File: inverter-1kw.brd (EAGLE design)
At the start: 160 x 100 mm, 242 parts, among them IC1 LM358D, IC5 ISO3082, IC6 25LC080SN, IC9 LM358D, Q2 1200980569**TRANS SMD NPN MMB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, Q3 1200980569**TRANS SMD NPN MMB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, Q4 1200980569**TRANS SMD NPN MMB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, Q6 1200980569**TRANS SMD NPN MMB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, U1 ACS712, U2 STM32F334C6, U3 1039-2088**AM1L-0505SH30-NZ A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, U4 ACS712, U5 SI8230, U6 SI8230, U7 ACS712, X1 MCV3, X2 RADE2, X3 RADE2, X7 RADE2, X8 RADE2

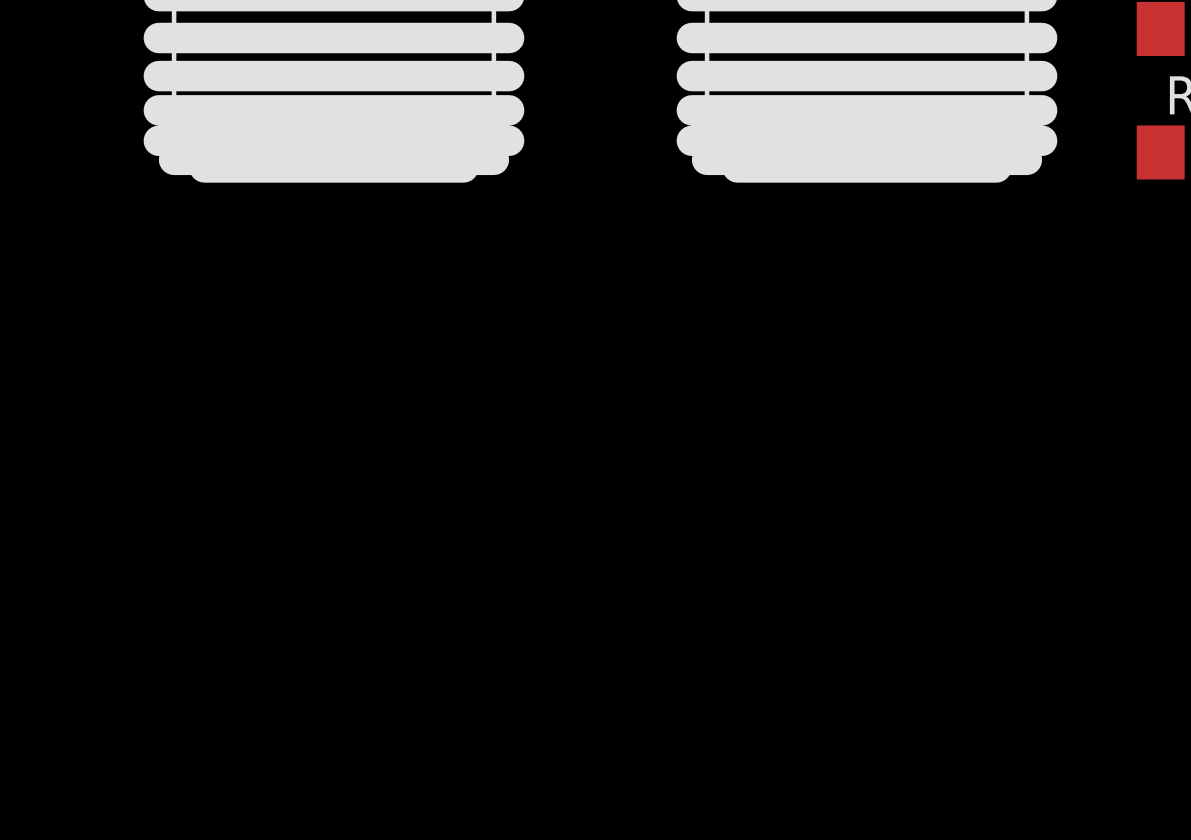
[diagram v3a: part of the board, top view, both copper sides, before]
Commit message: Cikis terminaline kondasator eklendi. Guc soketleri icin(4-pinli) kullanilacak urun linki value alanlarina yazildi.
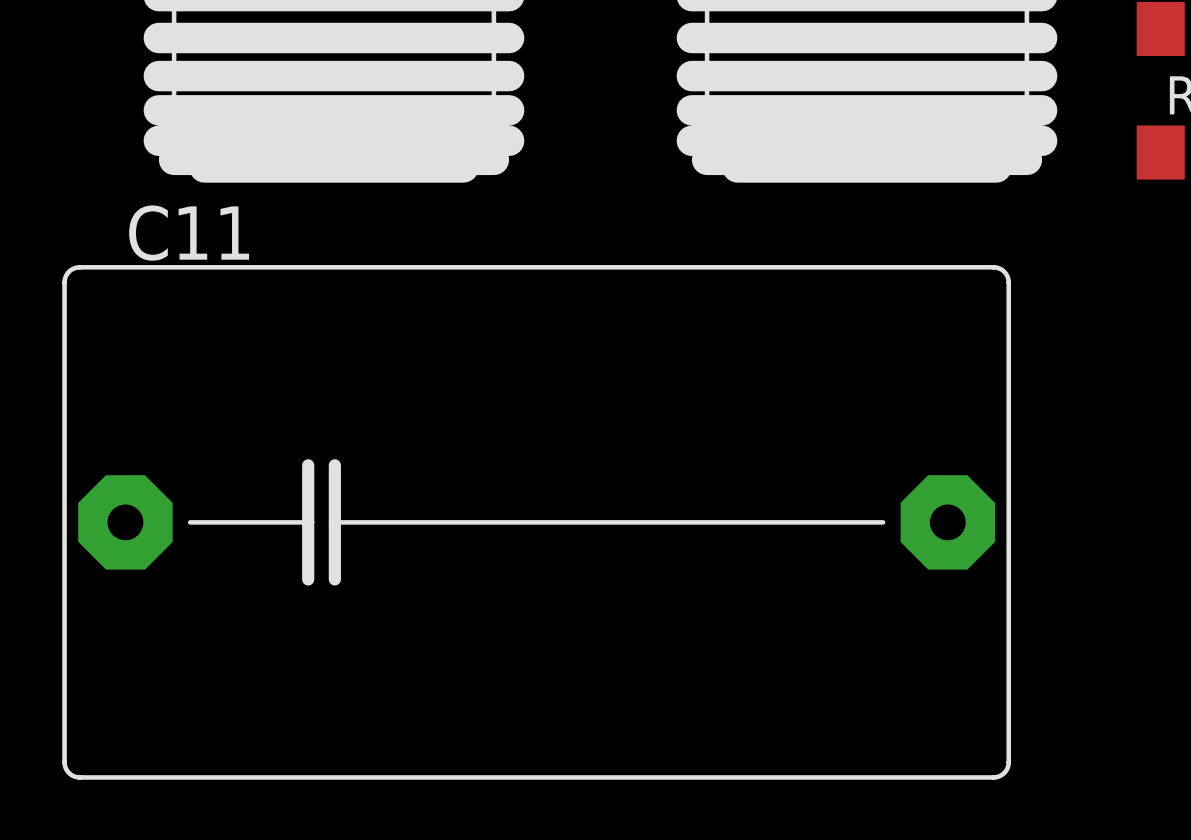
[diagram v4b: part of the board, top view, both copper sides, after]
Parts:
- added C11: (no value), capacitor-wima:C27.5B17
- X2, X3, X7, X8: value RADE2 -> https://ozdisan.com/connectors-and-interconnects/terminals/screw-connectors/K93-01AH
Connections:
- net N$1: now also C11.2
- net N$2: now also C11.1
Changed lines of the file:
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@@
 <layer number="250" name="Descript" color="3" fill="1" visible="no" active="no"/>
 <layer number="251" name="SMDround" color="12" fill="11" visible="no" active="no"/>
+<layer number="253" name="Extra" color="7" fill="1" visible="yes" active="yes"/>
 <layer number="254" name="cooling" color="7" fill="1" visible="yes" active="yes"/>
 <layer number="255" name="routoute" color="7" fill="1" visible="yes" active="yes"/>
@@
 <attribute name="VALUE" x="-65.913" y="99.695" size="1.27" layer="27" rot="R90"/>
 </element>
-<element name="IC5" library="enko" package="ISO3082" value="ISO3082" x="-74.93" y="87.63" smashed="yes">
+<element name="IC5" library="enko" library_urn="urn:adsk.eagle:library:26770947" package="ISO3082" package3d_urn="urn:adsk.eagle:package:26772954/1" value="ISO3082" x="-74.93" y="87.63" smashed="yes">
 <attribute name="NAME" x="-78.175" y="85.5" size="1.27" layer="25"/>
 <attribute name="VALUE" x="-78.175" y="88.69" size="1.27" layer="27"/>
@@
 <attribute name="VALUE" x="-54.61" y="203.835" size="1.27" layer="27"/>
 </element>
-<element name="L4" library="enko" package="ACM2012-900--2P-T002" value="ACM2012-900--2P-T002" x="-166.37" y="109.22" smashed="yes">
+<element name="L4" library="enko" library_urn="urn:adsk.eagle:library:26770947" package="ACM2012-900--2P-T002" package3d_urn="urn:adsk.eagle:package:26773148/1" value="ACM2012-900--2P-T002" x="-166.37" y="109.22" smashed="yes">
 <attribute name="NAME" x="-170.46" y="113.37" size="1.778" layer="25"/>
 <attribute name="VALUE" x="-170.99" y="110.99" size="1.778" layer="27"/>
 </element>
-<element name="L6" library="enko" package="ARYA_COMMON_FILTER" value="ARYA_COMMON_FILTER" x="-19.05" y="102.87" smashed="yes">
+<element name="L6" library="enko" library_urn="urn:adsk.eagle:library:26770947" package="ARYA_COMMON_FILTER" package3d_urn="urn:adsk.eagle:package:26773388/1" value="ARYA_COMMON_FILTER" x="-19.05" y="102.87" smashed="yes">
 <attribute name="NAME" x="-18.288" y="107.442" size="1.27" layer="25" rot="R180"/>
 <attribute name="VALUE" x="-17.018" y="99.568" size="1.27" layer="27" rot="R180"/>
 </element>
-<element name="L7" library="enko" package="ARYA_COMMON_FILTER" value="ARYA_COMMON_FILTER" x="-44.45" y="102.87" smashed="yes">
+<element name="L7" library="enko" library_urn="urn:adsk.eagle:library:26770947" package="ARYA_COMMON_FILTER" package3d_urn="urn:adsk.eagle:package:26773388/1" value="ARYA_COMMON_FILTER" x="-44.45" y="102.87" smashed="yes">
 <attribute name="NAME" x="-43.688" y="107.442" size="1.27" layer="25" rot="R180"/>
 <attribute name="VALUE" x="-42.418" y="99.568" size="1.27" layer="27" rot="R180"/>
@@
 <attribute name="VALUE" x="-48.26" y="82.296" size="1.778" layer="27" ratio="10"/>
 </element>
-<element name="X2" library="enko" package="RADE2" value="RADE2" x="-135.89" y="87.63" smashed="yes">
+<element name="X2" library="enko" library_urn="urn:adsk.eagle:library:26770947" package="RADE2" package3d_urn="urn:adsk.eagle:package:26773267/1" value="https://ozdisan.com/connectors-and-interconnects/terminals/screw-connectors/K93-01AH" x="-135.89" y="87.63" smashed="yes">
 <attribute name="NAME" x="-138.0643" y="82.5361" size="1.27" layer="25" rot="R90"/>
 <attribute name="VALUE" x="-132.4243" y="82.5361" size="1.27" layer="27" rot="R90"/>
 </element>
-<element name="X3" library="enko" package="RADE2" value="RADE2" x="-144.78" y="87.63" smashed="yes">
+<element name="X3" library="enko" library_urn="urn:adsk.eagle:library:26770947" package="RADE2" package3d_urn="urn:adsk.eagle:package:26773267/1" value="https://ozdisan.com/connectors-and-interconnects/terminals/screw-connectors/K93-01AH" x="-144.78" y="87.63" smashed="yes">
 <attribute name="NAME" x="-146.9543" y="82.5361" size="1.27" layer="25" rot="R90"/>
 <attribute name="VALUE" x="-141.3143" y="82.5361" size="1.27" layer="27" rot="R90"/>
 </element>
-<element name="X7" library="enko" package="RADE2" value="RADE2" x="2.21" y="87.88" smashed="yes" rot="R180">
+<element name="X7" library="enko" library_urn="urn:adsk.eagle:library:26770947" package="RADE2" package3d_urn="urn:adsk.eagle:package:26773267/1" value="https://ozdisan.com/connectors-and-interconnects/terminals/screw-connectors/K93-01AH" x="2.21" y="87.88" smashed="yes" rot="R180">
 <attribute name="NAME" x="4.3843" y="92.9739" size="1.27" layer="25" rot="R270"/>
 <attribute name="VALUE" x="-1.2557" y="92.9739" size="1.27" layer="27" rot="R270"/>
 </element>
-<element name="X8" library="enko" package="RADE2" value="RADE2" x="2.34" y="77.06" smashed="yes" rot="R180">
+<element name="X8" library="enko" library_urn="urn:adsk.eagle:library:26770947" package="RADE2" package3d_urn="urn:adsk.eagle:package:26773267/1" value="https://ozdisan.com/connectors-and-interconnects/terminals/screw-connectors/K93-01AH" x="2.34" y="77.06" smashed="yes" rot="R180">
 <attribute name="NAME" x="4.5143" y="82.1539" size="1.27" layer="25" rot="R270"/>
 <attribute name="VALUE" x="-1.1257" y="82.1539" size="1.27" layer="27" rot="R270"/>
@@
 <attribute name="SPICEPREFIX" value="L" x="-202.31" y="-18.06" size="1.778" layer="27" display="off"/>
 <attribute name="VALUE" x="-194.182" y="-15.52" size="1.27" layer="27" ratio="10" rot="R90"/>
+</element>
+<element name="C11" library="capacitor-wima" library_urn="urn:adsk.eagle:library:116" package="C27.5B17" package3d_urn="urn:adsk.eagle:package:5418/1" value="" x="-195.55" y="-41.33" smashed="yes">
+<attribute name="NAME" x="-209.266" y="-32.567" size="1.778" layer="25" ratio="10"/>
+<attribute name="POPULARITY" value="0" x="-195.55" y="-41.33" size="1.778" layer="27" display="off"/>
+<attribute name="VALUE" x="-200.63" y="-43.87" size="1.778" layer="27" ratio="10"/>
 </element>
 </elements>
@@
 <wire x1="-63.82" y1="120.82" x2="-67.945" y2="98.8" width="0" layer="19" extent="1-1"/>
 <wire x1="-128.27" y1="85.09" x2="-102.87" y2="85.09" width="0" layer="19" extent="1-1"/>
+<wire x1="-30.48" y1="2.215" x2="-53.86" y2="84.65" width="0" layer="19" extent="1-1"/>
 <wire x1="36.74" y1="65.345" x2="-15.06" y2="137.16" width="0" layer="19" extent="1-1"/>
 <wire x1="89.24" y1="68.88" x2="41.85" y2="65.83" width="0" layer="19" extent="1-1"/>
 <wire x1="110.22" y1="69.95" x2="89.24" y2="68.88" width="0" layer="19" extent="1-1"/>
-<wire x1="-30.48" y1="2.215" x2="-53.86" y2="84.65" width="0" layer="19" extent="1-1"/>
 </signal>
 <signal name="V_IN">
@@
 <contactref element="X2" pad="1"/>
 <contactref element="R26" pad="1"/>
-<wire x1="-89.515" y1="99" x2="-133.502" y2="218.44" width="0" layer="19" extent="1-1"/>
+<contactref element="C11" pad="2"/>
+<wire x1="-135.89" y1="85.09" x2="-181.834" y2="-41.33" width="0" layer="19" extent="1-1"/>
+<wire x1="-135.89" y1="90.17" x2="-135.89" y2="85.09" width="0" layer="19" extent="1-1"/>
+<wire x1="-89.515" y1="99" x2="-135.89" y2="90.17" width="0" layer="19" extent="1-1"/>
 <wire x1="-88.245" y1="99" x2="-89.515" y2="99" width="0" layer="19" extent="1-1"/>
-<wire x1="-135.89" y1="90.17" x2="-89.515" y2="99" width="0" layer="19" extent="1-1"/>
-<wire x1="-135.89" y1="85.09" x2="-135.89" y2="90.17" width="0" layer="19" extent="1-1"/>
+<wire x1="-133.502" y1="218.44" x2="-89.515" y2="99" width="0" layer="19" extent="1-1"/>
 </signal>
 <signal name="N$2">
@@
 <contactref element="X3" pad="1"/>
 <contactref element="R23" pad="2"/>
-<wire x1="-109.835" y1="99" x2="-115.418" y2="218.44" width="0" layer="19" extent="1-1"/>
+<contactref element="C11" pad="1"/>
+<wire x1="-144.78" y1="85.09" x2="-209.266" y2="-41.33" width="0" layer="19" extent="1-1"/>
+<wire x1="-144.78" y1="90.17" x2="-144.78" y2="85.09" width="0" layer="19" extent="1-1"/>
+<wire x1="-109.835" y1="99" x2="-144.78" y2="90.17" width="0" layer="19" extent="1-1"/>
 <wire x1="-108.565" y1="99" x2="-109.835" y2="99" width="0" layer="19" extent="1-1"/>
-<wire x1="-144.78" y1="90.17" x2="-109.835" y2="99" width="0" layer="19" extent="1-1"/>
-<wire x1="-144.78" y1="85.09" x2="-144.78" y2="90.17" width="0" layer="19" extent="1-1"/>
+<wire x1="-115.418" y1="218.44" x2="-109.835" y2="99" width="0" layer="19" extent="1-1"/>
 </signal>
 <signal name="VIN">

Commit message: Opamp paketleri ve etrafindaki malzemeler kucultuldu.
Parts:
- removed IC9: LM358D, linear:SO08
- added C12, C13: 150pF, rcl:C0603
- added C18, C19: (no value), rcl:C0603
- added IC2: LMV358MMX, linear:MSOP08
- added R100, R101, R99: 2k, rcl:R0603
- C114, C20, C23, C24: device rcl:C0805 -> rcl:C0603
- C14, C15, C21, C22, C38, C39: device rcl:C1206 -> rcl:C0603
- IC1: value LM358D -> LMV358MMX; device linear:SO08 -> linear:MSOP08
- R10, R16, R17, R9: device rcl:R1206 -> rcl:R0603
- R18, R4: device rcl:R0805 -> rcl:R0603
- moved IC1 215.4 mm to (-215.4, -57.1)
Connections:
- removed net GND_R: R15.1
- removed net V_LEFT: R3.1
- removed net V_RIGHT: R12.1
- new net VA_OUT: C11.1, R12.1, R23.2, U7.3, U7.4, X3.1, X3.2
- new net VB_OUT: C11.2, R15.1, R26.1, U1.3, U1.4, X2.1, X2.2
- new net VIN_SENS_DIFF: C20.1, R4.2
- new net VOUT_DIFF: C23.1, R18.2
- net +3V3: now also IC2.8, R100.2; no longer IC9.8
- net AGND: now also R7.1
- net DGND: now also C18.2, C19.2, IC2.4, R101.1; no longer IC9.4
- net GND_L: no longer R7.1
- net N$1: now also C19.1, IC2.3, R100.1, R101.2; no longer C11.2, R26.1, U1.3, U1.4, X2.1, X2.2
- net N$18: now also C13.2
- net N$2: now also IC2.1, IC2.2, R99.1; no longer C11.1, R23.2, U7.3, U7.4, X3.1, X3.2
- net N$20: now also IC1.5; no longer IC9.3
- net N$23: now also C12.1, IC1.6; no longer IC9.2
- net N$25: now also C12.2, IC1.7; no longer IC9.1
- net N$9: now also C13.1
- net VIN: now also R3.1
- net VREF: now also C18.1, R99.2
- net V_LEFT_MESURE: no longer C20.1, R4.2
- net V_RIGHT_MESURE: no longer C23.1, R18.2

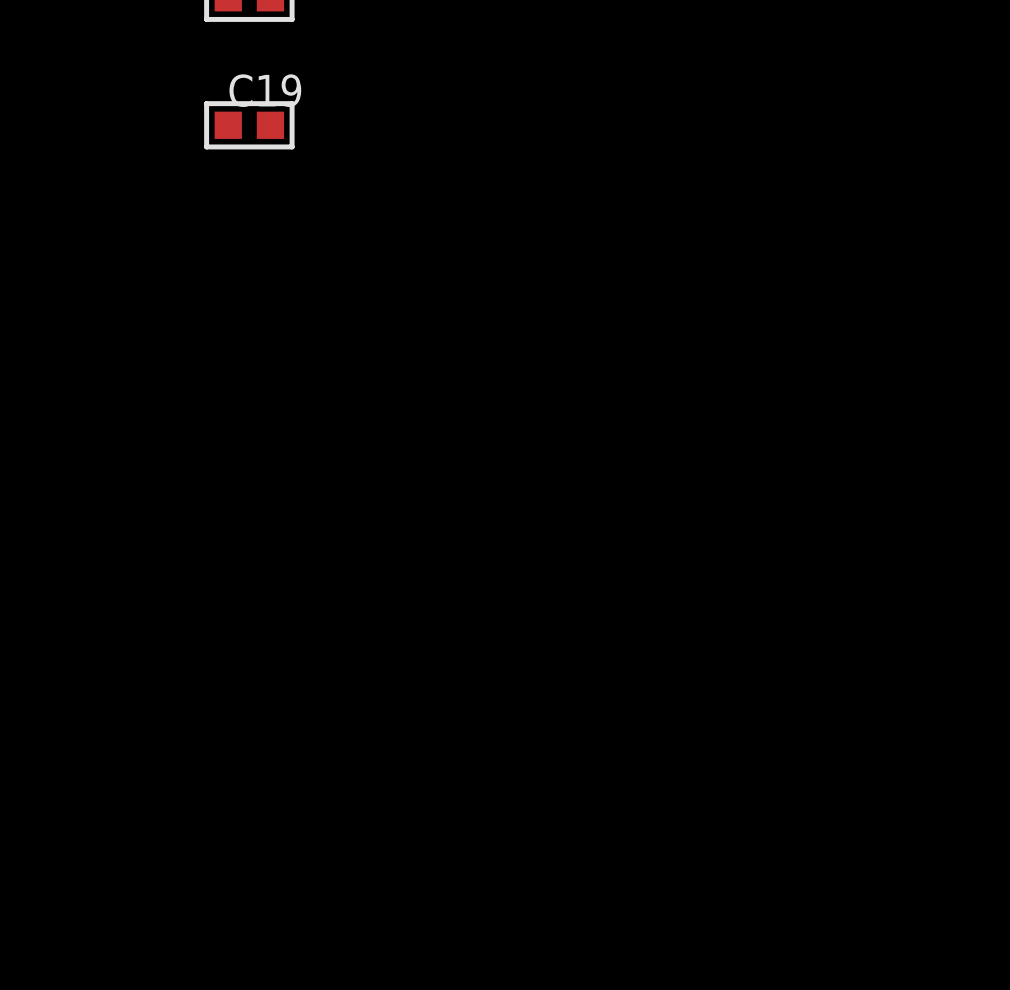
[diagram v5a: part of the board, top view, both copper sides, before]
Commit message: Kontrol karti soketleri eklendi.
Giris beslemesini gostermek icin led eklentisi yapildi.
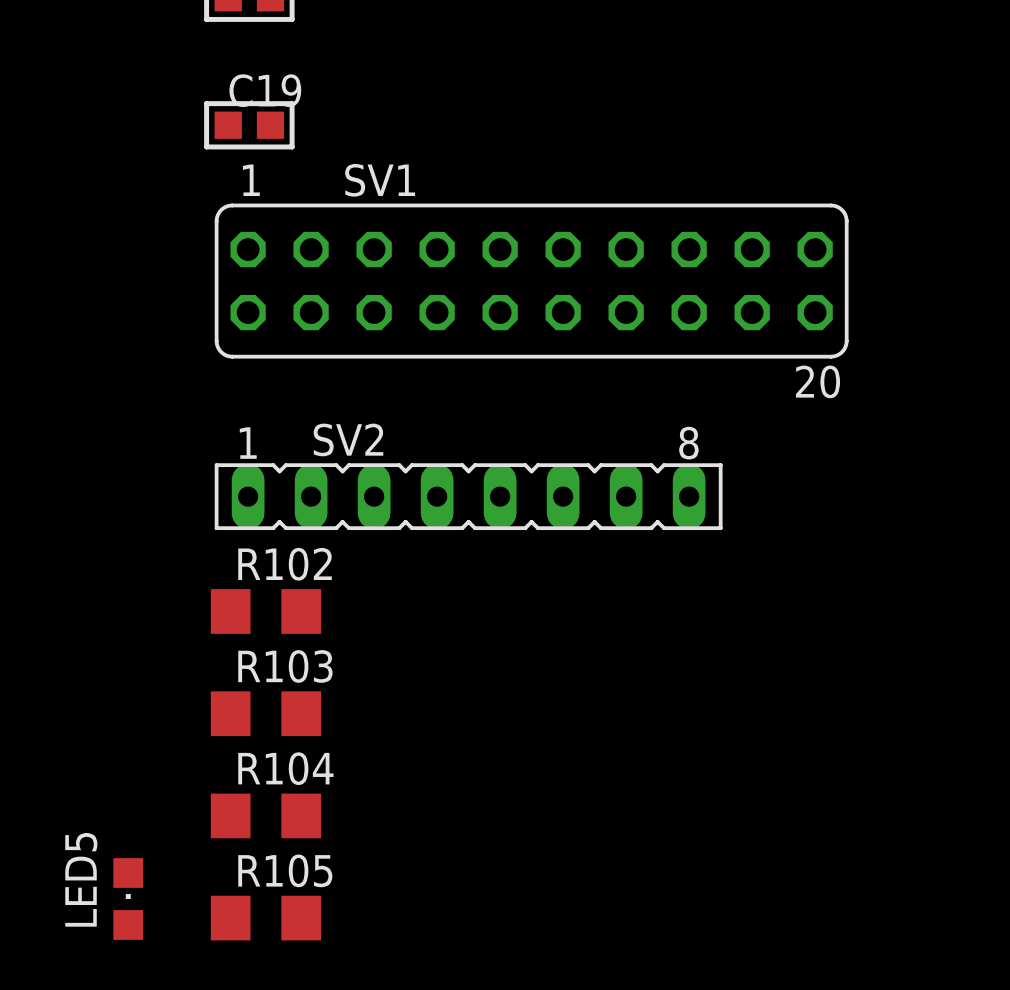
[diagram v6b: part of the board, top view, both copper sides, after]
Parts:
- added LED5: (no value), led:CHIPLED_0805
- added R102, R103, R104, R105: (no value), rcl:R1206
- added SV1: (no value), con-lsta:FE10-2
- added SV2: (no value), con-lsta:FE08
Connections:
- removed net VOUT_DIFF: C23.1, R18.2
- new net FAN: SV1.14
- new net N$54: R102.1, R103.2
- new net N$56: R103.1, R104.2
- new net N$58: R104.1, R105.2
- new net N$68: LED5.A, R105.1
- new net NTC-HS1: SV1.16
- new net NTC-HS2: SV1.18
- new net POWER_IN: SV2.1
- new net VOUT_SENS_DIFF: C23.1, R18.2, SV1.1
- net +3V3: now also SV2.7
- net +5V: now also SV2.5
- net AGND: now also LED5.C, SV2.3
- net DGND: now also SV2.6, SV2.8
- net G11_PWM: now also SV1.2
- net G12_PWM: now also SV1.4
- net G13_PWM: now also SV1.6
- net G14_PWM: now also SV1.8
- net IA_SENS: now also SV1.9
- net IB_SENS: now also SV1.11
- net IIN_SENS: now also SV1.5
- net RELAY1: now also SV1.10
- net RELAY2: now also SV1.12
- net VA_SENS: now also SV1.13
- net VB_SENS: now also SV1.15
- net VDD: now also SV2.4
- net VIN: now also R102.2
- net VIN_SENS: now also SV1.7
- net VIN_SENS_DIFF: now also SV1.3

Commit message: Guc hattinda bulunmayan bir cok cap paketi 603 yapildi.
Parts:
- C10, C139, C140, C144, C145, C16, C17, C25, C26, C72, C73, C75, C76, C87, C88, C89, C9, C90: device rcl:C0805 -> rcl:C0603
- R36, R41: device rcl:R0805 -> rcl:R0603
